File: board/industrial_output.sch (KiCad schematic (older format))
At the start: 3 parts

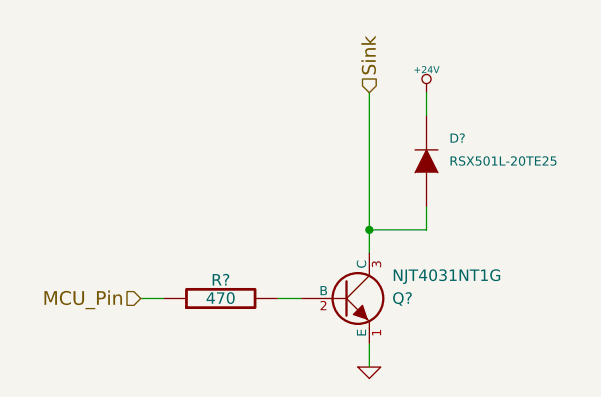
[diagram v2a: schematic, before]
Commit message: Fixed ERC Errors. Annotated all components.
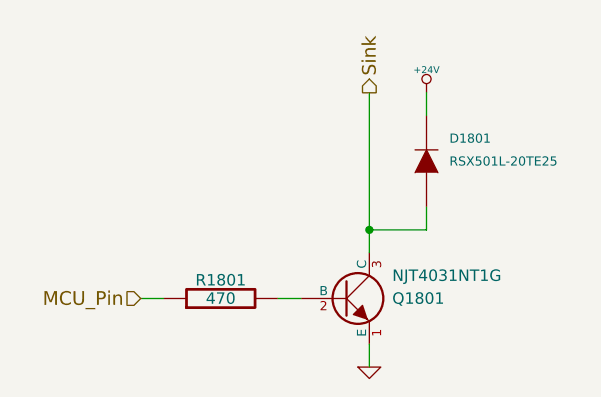
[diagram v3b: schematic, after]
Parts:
- gave numbers to parts that had none: 3
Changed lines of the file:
@@
 $Descr A 11000 8500
 encoding utf-8
-Sheet 19 26
+Sheet 18 26
 Title "Industrial Digital Output"
 Date ""
@@
 $EndDescr
 $Comp
-L NPN Q?
+L NPN Q1501
 U 1 1 52E6FDE0
 P 5450 4500
-F 0 "Q?" H 5650 4500 50  0000 L CNN
+AR Path="/52FAAFCB/52E6FDE0" Ref="Q1501"  Part="1"
+AR Path="/52FAC46B/52E6FDE0" Ref="Q1601"  Part="1"
+AR Path="/52FAD3BD/52E6FDE0" Ref="Q1701"  Part="1"
+AR Path="/52FAD3C1/52E6FDE0" Ref="Q1801"  Part="1"
+AR Path="/52FAF26D/52E6FDE0" Ref="Q1901"  Part="1"
+AR Path="/52FAF271/52E6FDE0" Ref="Q2001"  Part="1"
+AR Path="/52FAF275/52E6FDE0" Ref="Q2101"  Part="1"
+AR Path="/52FAF279/52E6FDE0" Ref="Q2201"  Part="1"
+F 0 "Q1801" H 5650 4500 50  0000 L CNN
 F 1 "NJT4031NT1G" H 5650 4600 50  0000 L CNN
 F 2 "" H 5450 4500 60  0000 C CNN
@@
 $EndComp
 $Comp
-L R R?
+L R R1501
 U 1 1 52E6FDF4
 P 4900 4500
-F 0 "R?" V 4980 4500 50  0000 C CNN
+AR Path="/52FAAFCB/52E6FDF4" Ref="R1501"  Part="1"
+AR Path="/52FAC46B/52E6FDF4" Ref="R1601"  Part="1"
+AR Path="/52FAD3BD/52E6FDF4" Ref="R1701"  Part="1"
+AR Path="/52FAD3C1/52E6FDF4" Ref="R1801"  Part="1"
+AR Path="/52FAF26D/52E6FDF4" Ref="R1901"  Part="1"
+AR Path="/52FAF271/52E6FDF4" Ref="R2001"  Part="1"
+AR Path="/52FAF275/52E6FDF4" Ref="R2101"  Part="1"
+AR Path="/52FAF279/52E6FDF4" Ref="R2201"  Part="1"
+F 0 "R1801" V 4980 4500 50  0000 C CNN
 F 1 "470" V 4900 4500 50  0000 C CNN
 F 2 "" H 4900 4500 60  0000 C CNN
@@
 	5150 4500 5250 4500
 $Comp
-L GND #PWR?
+L GND #PWR0160
 U 1 1 52E6FE0A
 P 5550 4800
-F 0 "#PWR?" H 5550 4800 30  0001 C CNN
+AR Path="/52FAAFCB/52E6FE0A" Ref="#PWR0160"  Part="1"
+AR Path="/52FAC46B/52E6FE0A" Ref="#PWR0162"  Part="1"
+AR Path="/52FAD3BD/52E6FE0A" Ref="#PWR0164"  Part="1"
+AR Path="/52FAD3C1/52E6FE0A" Ref="#PWR0166"  Part="1"
+AR Path="/52FAF26D/52E6FE0A" Ref="#PWR0168"  Part="1"
+AR Path="/52FAF271/52E6FE0A" Ref="#PWR0170"  Part="1"
+AR Path="/52FAF275/52E6FE0A" Ref="#PWR0172"  Part="1"
+AR Path="/52FAF279/52E6FE0A" Ref="#PWR0174"  Part="1"
+F 0 "#PWR0174" H 5550 4800 30  0001 C CNN
 F 1 "GND" H 5550 4730 30  0001 C CNN
 F 2 "" H 5550 4800 60  0000 C CNN
@@
 Wire Wire Line
 	5550 3600 5550 4300
-Text HLabel 5550 3600 1    60   Input ~ 0
+Text HLabel 5550 3600 1    60   Output ~ 0
 Sink
 $Comp
-L DIODE D?
+L DIODE D1501
 U 1 1 52E705F0
 P 5800 3900
-F 0 "D?" V 5900 3800 40  0000 R CNN
+AR Path="/52FAAFCB/52E705F0" Ref="D1501"  Part="1"
+AR Path="/52FAC46B/52E705F0" Ref="D1601"  Part="1"
+AR Path="/52FAD3BD/52E705F0" Ref="D1701"  Part="1"
+AR Path="/52FAD3C1/52E705F0" Ref="D1801"  Part="1"
+AR Path="/52FAF26D/52E705F0" Ref="D1901"  Part="1"
+AR Path="/52FAF271/52E705F0" Ref="D2001"  Part="1"
+AR Path="/52FAF275/52E705F0" Ref="D2101"  Part="1"
+AR Path="/52FAF279/52E705F0" Ref="D2201"  Part="1"
+F 0 "D1801" V 5900 3800 40  0000 R CNN
 F 1 "RSX501L-20TE25" V 5800 3800 40  0000 R CNN
 F 2 "" H 5800 3900 60  0000 C CNN
@@
 Connection ~ 5550 4200
 $Comp
-L +24V #PWR?
+L +24V #PWR0161
 U 1 1 52E70673
 P 5800 3600
-F 0 "#PWR?" H 5800 3550 20  0001 C CNN
+AR Path="/52FAAFCB/52E70673" Ref="#PWR0161"  Part="1"
+AR Path="/52FAC46B/52E70673" Ref="#PWR0163"  Part="1"
+AR Path="/52FAD3BD/52E70673" Ref="#PWR0165"  Part="1"
+AR Path="/52FAD3C1/52E70673" Ref="#PWR0167"  Part="1"
+AR Path="/52FAF26D/52E70673" Ref="#PWR0169"  Part="1"
+AR Path="/52FAF271/52E70673" Ref="#PWR0171"  Part="1"
+AR Path="/52FAF275/52E70673" Ref="#PWR0173"  Part="1"
+AR Path="/52FAF279/52E70673" Ref="#PWR0175"  Part="1"
+F 0 "#PWR0175" H 5800 3550 20  0001 C CNN
 F 1 "+24V" H 5800 3700 30  0000 C CNN
 F 2 "" H 5800 3600 60  0000 C CNN
